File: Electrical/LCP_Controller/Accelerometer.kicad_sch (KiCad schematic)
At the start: 6 parts, among them J6 SALEAE_TEST, U10 LIS2DW12

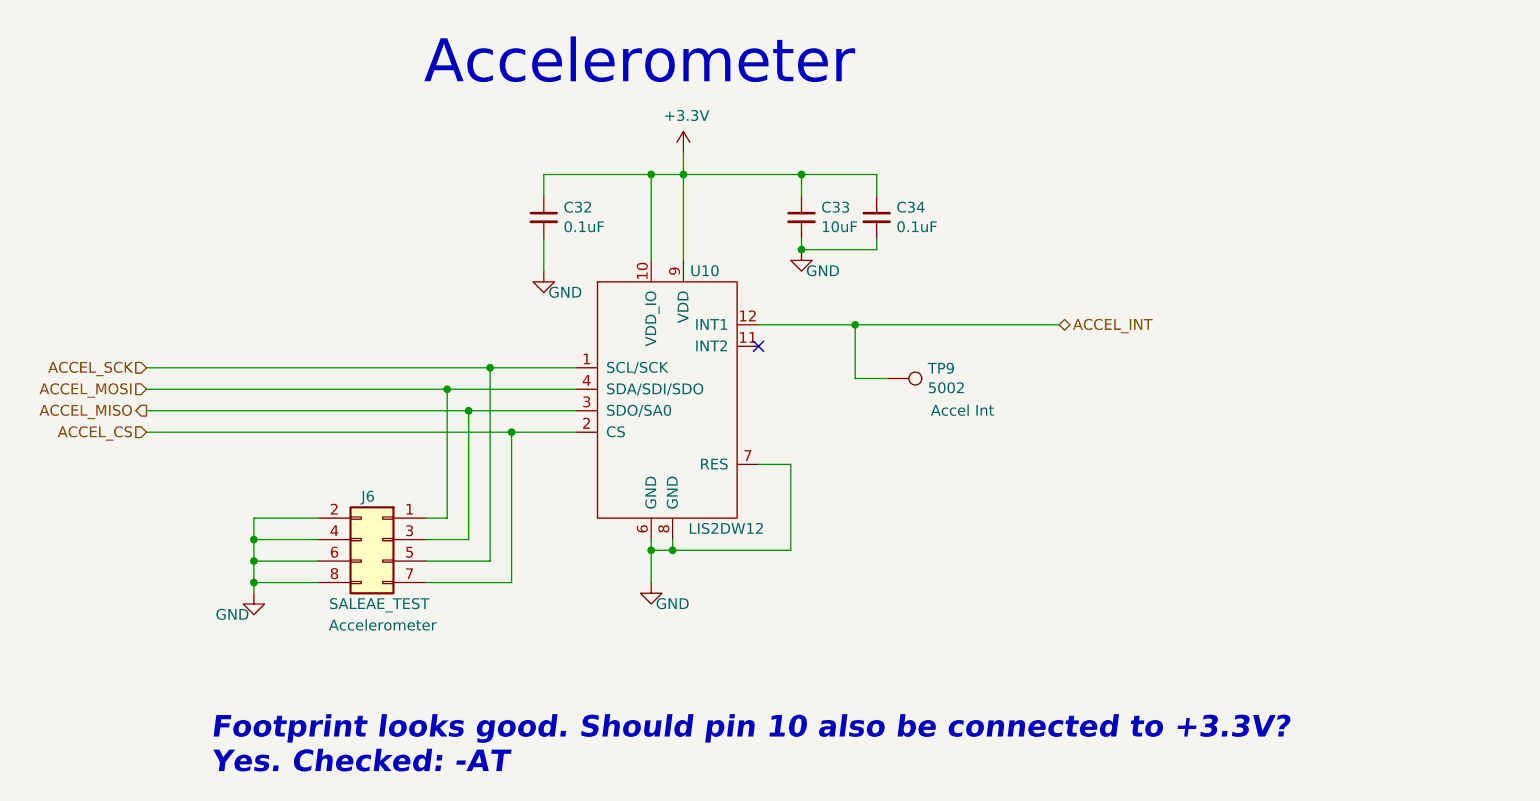
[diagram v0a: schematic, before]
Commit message: Hardware Revision : v0.3
1. modified schematic design, removed unnecessary test points.
2. pcb layout 2x8 Inches allowance dimension, layout is in progress
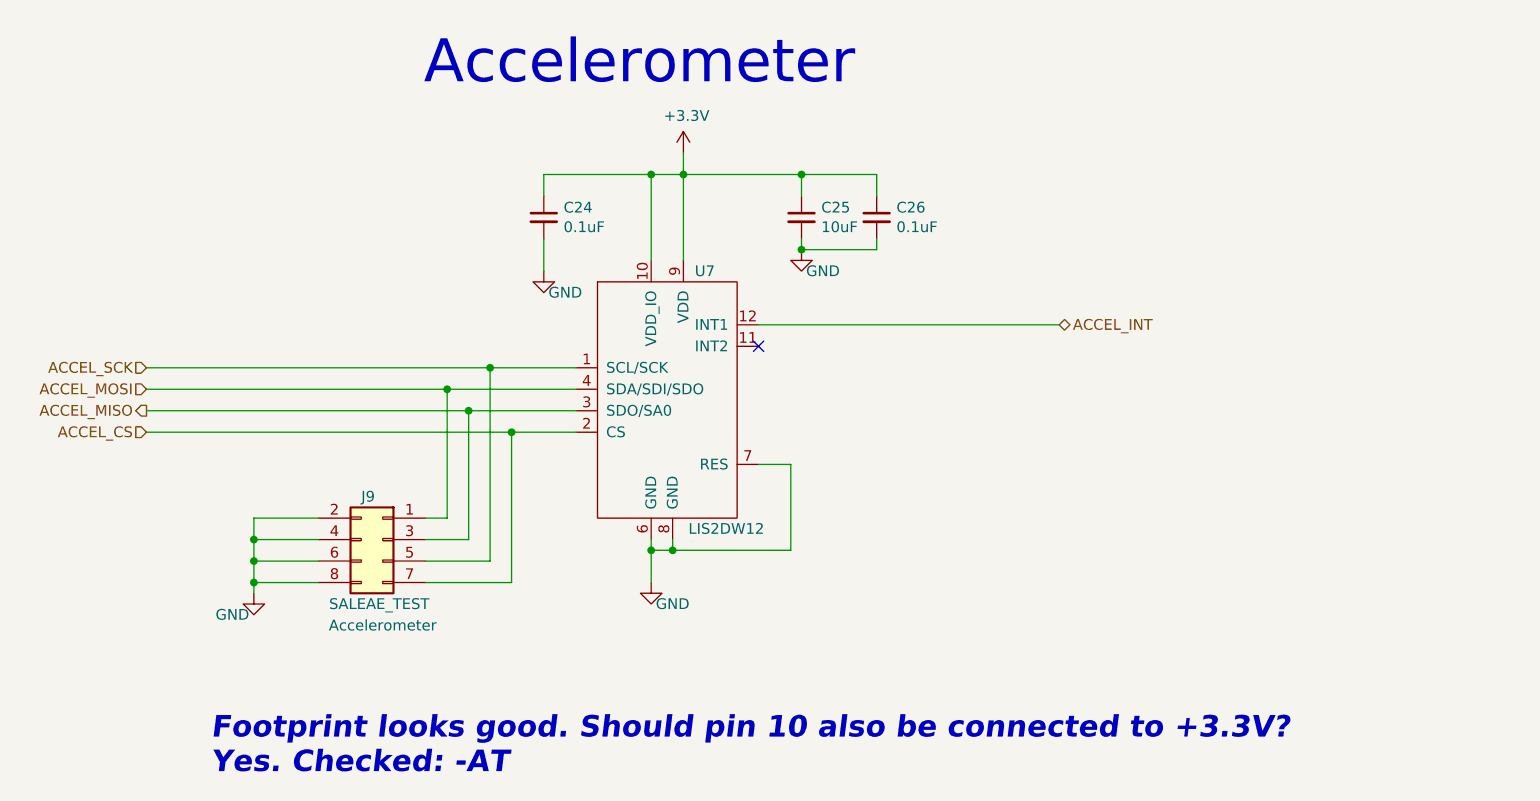
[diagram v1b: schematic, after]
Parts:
- removed TP9: 5002, TestPoint:TestPoint_Keystone_5000-5004_Miniature, symbol Connector:TestPoint
- renumbered C32 to C24, C33 to C25, C34 to C26, J6 to J9, U10 to U7
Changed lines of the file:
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@@
   (junction (at 157.48 119.38) (diameter 0) (color 0 0 0 0)
   )
-  (junction (at 179.07 92.71) (diameter 0) (color 0 0 0 0)
-  )
   (junction (at 107.95 120.65) (diameter 0) (color 0 0 0 0)
   )
@@
   )
   (no_connect (at 167.64 95.25))
-  (wire (pts (xy 182.88 99.06) (xy 179.07 99.06))
-    (stroke (width 0) (type default) (color 0 0 0 0))
-  )
   (wire (pts (xy 138.43 123.19) (xy 138.43 105.41))
     (stroke (width 0) (type default) (color 0 0 0 0))
@@
     (stroke (width 0) (type default) (color 0 0 0 0))
   )
-  (wire (pts (xy 179.07 92.71) (xy 203.2 92.71))
+  (wire (pts (xy 167.64 92.71) (xy 203.2 92.71))
     (stroke (width 0) (type default) (color 0 0 0 0))
   )
@@
     (stroke (width 0) (type default) (color 0 0 0 0))
   )
-  (wire (pts (xy 167.64 92.71) (xy 179.07 92.71))
-    (stroke (width 0) (type default) (color 0 0 0 0))
-  )
   (wire (pts (xy 181.61 74.93) (xy 181.61 77.47))
     (stroke (width 0) (type default) (color 0 0 0 0))
@@
   )
   (wire (pts (xy 95.25 102.87) (xy 133.35 102.87))
-    (stroke (width 0) (type default) (color 0 0 0 0))
-  )
-  (wire (pts (xy 179.07 99.06) (xy 179.07 92.71))
     (stroke (width 0) (type default) (color 0 0 0 0))
   )
@@
     (effects (font (size 1.27 1.27)) (justify left))
   )
-  (symbol (lib_id "Connector:TestPoint") (at 182.88 99.06 270) (unit 1)
-    (in_bom yes) (on_board yes)
-    (property "Reference" "TP9" (id 0) (at 187.6552 97.8916 90)
-      (effects (font (size 1.27 1.27)) (justify left))
-    )
-    (property "Value" "5002" (id 1) (at 187.6552 100.203 90)
-      (effects (font (size 1.27 1.27)) (justify left))
-    )
-    (property "Footprint" "TestPoint:TestPoint_Keystone_5000-5004_Miniature" (id 2) (at 182.88 104.14 0)
-      (effects (font (size 1.27 1.27)) hide)
-    )
-    (property "Datasheet" "~" (id 3) (at 182.88 104.14 0)
-      (effects (font (size 1.27 1.27)) hide)
-    )
-    (property "TestPoint" "Accel Int" (id 4) (at 191.77 102.87 90))
-    (property "MPN" "" (id 5) (at 182.88 99.06 0)
-      (effects (font (size 1.27 1.27)) hide)
-    )
-    (pin "1")
-  )
   (symbol (lib_id "Connector_Generic:Conn_02x04_Odd_Even") (at 123.19 118.11 0) (mirror y) (unit 1)
     (in_bom yes) (on_board yes)
-    (property "Reference" "J6" (id 0) (at 120.65 113.03 0)
+    (property "Reference" "J9" (id 0) (at 120.65 113.03 0)
       (effects (font (size 1.27 1.27)) (justify right))
     )
@@
   (symbol (lib_id "power:GND") (at 107.95 124.46 0) (unit 1)
     (in_bom yes) (on_board yes)
-    (property "Reference" "#PWR052" (id 0) (at 107.95 130.81 0)
+    (property "Reference" "#PWR058" (id 0) (at 107.95 130.81 0)
       (effects (font (size 1.27 1.27)) hide)
     )
@@
   (symbol (lib_id "power:GND") (at 154.94 123.19 0) (unit 1)
     (in_bom yes) (on_board yes)
-    (property "Reference" "#PWR054" (id 0) (at 154.94 129.54 0)
+    (property "Reference" "#PWR057" (id 0) (at 154.94 129.54 0)
       (effects (font (size 1.27 1.27)) hide)
     )
@@
   (symbol (lib_id "Device:C_Small") (at 142.24 80.01 0) (unit 1)
     (in_bom yes) (on_board yes)
-    (property "Reference" "C32" (id 0) (at 144.5768 78.8416 0)
+    (property "Reference" "C24" (id 0) (at 144.5768 78.8416 0)
       (effects (font (size 1.27 1.27)) (justify left))
     )
@@
   (symbol (lib_id "power:GND") (at 142.24 86.36 0) (unit 1)
     (in_bom yes) (on_board yes)
-    (property "Reference" "#PWR053" (id 0) (at 142.24 92.71 0)
+    (property "Reference" "#PWR056" (id 0) (at 142.24 92.71 0)
       (effects (font (size 1.27 1.27)) hide)
     )
@@
   (symbol (lib_id "power:+3.3V") (at 158.75 72.39 0) (unit 1)
     (in_bom yes) (on_board yes)
-    (property "Reference" "#PWR055" (id 0) (at 158.75 76.2 0)
+    (property "Reference" "#PWR054" (id 0) (at 158.75 76.2 0)
       (effects (font (size 1.27 1.27)) hide)
     )
@@
   (symbol (lib_id "PMEL_Sensors:LIS2DW12") (at 157.48 104.14 0) (unit 1)
     (in_bom yes) (on_board yes)
-    (property "Reference" "U10" (id 0) (at 161.29 86.36 0))
+    (property "Reference" "U7" (id 0) (at 161.29 86.36 0))
     (property "Value" "LIS2DW12" (id 1) (at 163.83 116.84 0))
     (property "Footprint" "Package_LGA:LGA-12_2x2mm_P0.5mm" (id 2) (at 157.48 116.84 0)
@@
   (symbol (lib_id "power:GND") (at 172.72 83.82 0) (unit 1)
     (in_bom yes) (on_board yes)
-    (property "Reference" "#PWR056" (id 0) (at 172.72 90.17 0)
+    (property "Reference" "#PWR055" (id 0) (at 172.72 90.17 0)
       (effects (font (size 1.27 1.27)) hide)
     )
@@
   (symbol (lib_id "Device:C_Small") (at 172.72 80.01 0) (unit 1)
     (in_bom yes) (on_board yes)
-    (property "Reference" "C33" (id 0) (at 175.0568 78.8416 0)
+    (property "Reference" "C25" (id 0) (at 175.0568 78.8416 0)
       (effects (font (size 1.27 1.27)) (justify left))
     )
@@
   (symbol (lib_id "Device:C_Small") (at 181.61 80.01 0) (unit 1)
     (in_bom yes) (on_board yes)
-    (property "Reference" "C34" (id 0) (at 183.9468 78.8416 0)
-      (effects (font (size 1.27 1.27)) (justify left))
-    )
+    (property "Reference" "C26" (id 0) (at 183.9468 78.8416 0)
+      (effects (font (size 1.27 1.27)) (justify left))
+    )

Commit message: Removed RF Switch
Deleted the RF Switch.

GPS Signal is routed to J17 and Iridium to J18.
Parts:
- J9: footprint Connector_PinHeader_2.54mm:PinHeader_2x04_P2.54mm_Vertical -> Connector_Molex:Molex_Micro-Fit_3.0_43045-0612_2x03_P3.00mm_Vertical

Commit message: GPS and Iridium Layout Finalized
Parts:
- J9: footprint Connector_Molex:Molex_Micro-Fit_3.0_43045-0612_2x03_P3.00mm_Vertical -> Connector_PinHeader_2.54mm:PinHeader_2x04_P2.54mm_Vertical
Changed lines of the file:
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@@
       (effects (font (size 1.27 1.27)) (justify right))
     )
-    (property "Footprint" "Connector_Molex:Molex_Micro-Fit_3.0_43045-0612_2x03_P3.00mm_Vertical" (at 123.19 118.11 0)
+    (property "Footprint" "Connector_PinHeader_2.54mm:PinHeader_2x04_P2.54mm_Vertical" (at 123.19 118.11 0)
       (effects (font (size 1.27 1.27)) hide)
     )

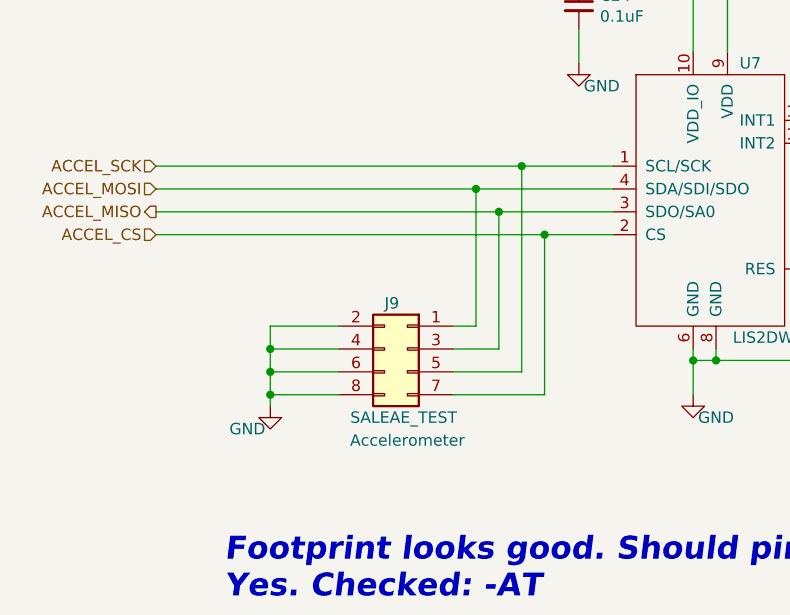
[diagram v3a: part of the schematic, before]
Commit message: Connector Progress
J2 J22 and J23 converted to Molex Microfit

SALEAE TEST connectors removed
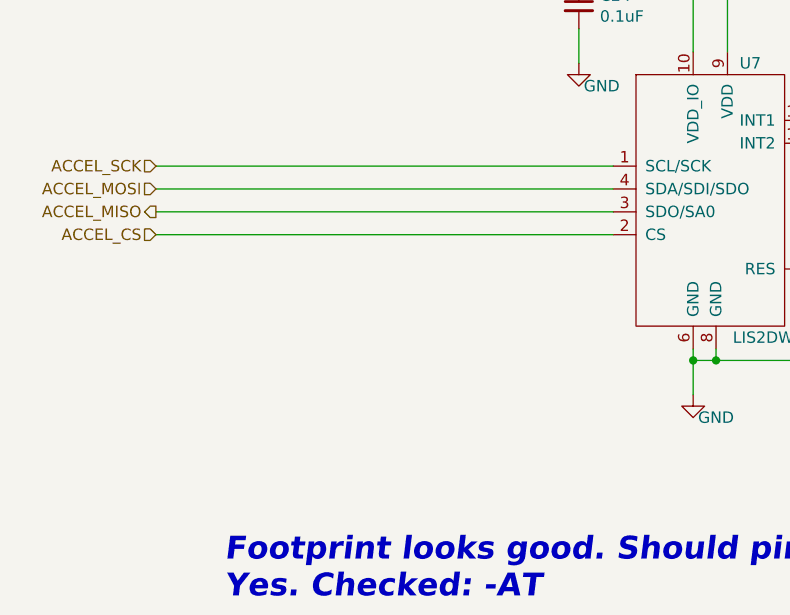
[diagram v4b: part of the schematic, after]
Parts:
- removed J9: SALEAE_TEST, Connector_PinHeader_2.54mm:PinHeader_2x04_P2.54mm_Vertical, symbol Connector_Generic:Conn_02x04_Odd_Even
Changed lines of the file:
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@@
     (comment 5 "Current design modified by: Basharat Martin")
   )
-  (junction (at 133.35 102.87) (diameter 0) (color 0 0 0 0)
-  )
-  (junction (at 135.89 97.79) (diameter 0) (color 0 0 0 0)
-  )
   (junction (at 154.94 74.93) (diameter 0) (color 0 0 0 0)
-  )
-  (junction (at 130.81 100.33) (diameter 0) (color 0 0 0 0)
-  )
-  (junction (at 107.95 123.19) (diameter 0) (color 0 0 0 0)
-  )
-  (junction (at 107.95 118.11) (diameter 0) (color 0 0 0 0)
   )
   (junction (at 172.72 83.82) (diameter 0) (color 0 0 0 0)
@@
   (junction (at 157.48 119.38) (diameter 0) (color 0 0 0 0)
   )
-  (junction (at 107.95 120.65) (diameter 0) (color 0 0 0 0)
-  )
-  (junction (at 138.43 105.41) (diameter 0) (color 0 0 0 0)
-  )
   (no_connect (at 167.64 95.25))
-  (wire (pts (xy 138.43 123.19) (xy 138.43 105.41))
-    (stroke (width 0) (type default))
-  )
   (wire (pts (xy 154.94 119.38) (xy 154.94 118.11))
     (stroke (width 0) (type default))
   )
   (wire (pts (xy 158.75 74.93) (xy 172.72 74.93))
-    (stroke (width 0) (type default))
-  )
-  (wire (pts (xy 146.05 97.79) (xy 135.89 97.79))
     (stroke (width 0) (type default))
   )
@@
     (stroke (width 0) (type default))
   )
-  (wire (pts (xy 128.27 120.65) (xy 135.89 120.65))
-    (stroke (width 0) (type default))
-  )
-  (wire (pts (xy 107.95 120.65) (xy 107.95 123.19))
-    (stroke (width 0) (type default))
-  )
   (wire (pts (xy 142.24 82.55) (xy 142.24 86.36))
-    (stroke (width 0) (type default))
-  )
-  (wire (pts (xy 107.95 115.57) (xy 115.57 115.57))
     (stroke (width 0) (type default))
   )
@@
     (stroke (width 0) (type default))
   )
-  (wire (pts (xy 107.95 118.11) (xy 107.95 115.57))
-    (stroke (width 0) (type default))
-  )
   (wire (pts (xy 142.24 74.93) (xy 142.24 77.47))
-    (stroke (width 0) (type default))
-  )
-  (wire (pts (xy 107.95 118.11) (xy 107.95 120.65))
     (stroke (width 0) (type default))
   )
@@
     (stroke (width 0) (type default))
   )
-  (wire (pts (xy 115.57 118.11) (xy 107.95 118.11))
-    (stroke (width 0) (type default))
-  )
-  (wire (pts (xy 115.57 120.65) (xy 107.95 120.65))
-    (stroke (width 0) (type default))
-  )
   (wire (pts (xy 171.45 109.22) (xy 167.64 109.22))
     (stroke (width 0) (type default))
@@
     (stroke (width 0) (type default))
   )
-  (wire (pts (xy 115.57 123.19) (xy 107.95 123.19))
-    (stroke (width 0) (type default))
-  )
   (wire (pts (xy 154.94 85.09) (xy 154.94 74.93))
     (stroke (width 0) (type default))
   )
-  (wire (pts (xy 95.25 100.33) (xy 130.81 100.33))
-    (stroke (width 0) (type default))
-  )
-  (wire (pts (xy 107.95 123.19) (xy 107.95 124.46))
+  (wire (pts (xy 95.25 100.33) (xy 146.05 100.33))
     (stroke (width 0) (type default))
   )
@@
     (stroke (width 0) (type default))
   )
-  (wire (pts (xy 130.81 115.57) (xy 130.81 100.33))
-    (stroke (width 0) (type default))
-  )
-  (wire (pts (xy 135.89 120.65) (xy 135.89 97.79))
-    (stroke (width 0) (type default))
-  )
-  (wire (pts (xy 128.27 123.19) (xy 138.43 123.19))
-    (stroke (width 0) (type default))
-  )
   (wire (pts (xy 157.48 118.11) (xy 157.48 119.38))
-    (stroke (width 0) (type default))
-  )
-  (wire (pts (xy 128.27 115.57) (xy 130.81 115.57))
     (stroke (width 0) (type default))
   )
@@
     (stroke (width 0) (type default))
   )
-  (wire (pts (xy 95.25 105.41) (xy 138.43 105.41))
-    (stroke (width 0) (type default))
-  )
-  (wire (pts (xy 146.05 100.33) (xy 130.81 100.33))
+  (wire (pts (xy 95.25 105.41) (xy 146.05 105.41))
     (stroke (width 0) (type default))
   )
@@
     (stroke (width 0) (type default))
   )
-  (wire (pts (xy 95.25 97.79) (xy 135.89 97.79))
-    (stroke (width 0) (type default))
-  )
-  (wire (pts (xy 128.27 118.11) (xy 133.35 118.11))
-    (stroke (width 0) (type default))
-  )
-  (wire (pts (xy 133.35 102.87) (xy 146.05 102.87))
+  (wire (pts (xy 95.25 97.79) (xy 146.05 97.79))
     (stroke (width 0) (type default))
   )
@@
     (stroke (width 0) (type default))
   )
-  (wire (pts (xy 95.25 102.87) (xy 133.35 102.87))
+  (wire (pts (xy 95.25 102.87) (xy 146.05 102.87))
     (stroke (width 0) (type default))
   )
   (wire (pts (xy 172.72 83.82) (xy 172.72 82.55))
-    (stroke (width 0) (type default))
-  )
-  (wire (pts (xy 133.35 118.11) (xy 133.35 102.87))
-    (stroke (width 0) (type default))
-  )
-  (wire (pts (xy 138.43 105.41) (xy 146.05 105.41))
     (stroke (width 0) (type default))
   )
@@
     (effects (font (size 1.27 1.27)) (justify left))
   )
-  (symbol (lib_id "Connector_Generic:Conn_02x04_Odd_Even") (at 123.19 118.11 0) (mirror y) (unit 1)
-    (in_bom yes) (on_board yes) (dnp no)
-    (property "Reference" "J9" (at 120.65 113.03 0)
-      (effects (font (size 1.27 1.27)) (justify right))
-    )
-    (property "Value" "SALEAE_TEST" (at 116.84 125.73 0)
-      (effects (font (size 1.27 1.27)) (justify right))
-    )
-    (property "Footprint" "Connector_PinHeader_2.54mm:PinHeader_2x04_P2.54mm_Vertical" (at 123.19 118.11 0)
-      (effects (font (size 1.27 1.27)) hide)
-    )
-    (property "Datasheet" "~" (at 123.19 118.11 0)
-      (effects (font (size 1.27 1.27)) hide)
-    )
-    (property "TestPoint" "Accelerometer" (at 123.19 128.27 0)
-      (effects (font (size 1.27 1.27)))
-    )
-    (property "MPN" "0010897080" (at 123.19 118.11 0)
-      (effects (font (size 1.27 1.27)) hide)
-    )
-    (pin "1")
-    (pin "2")
-    (pin "3")
-    (pin "4")
-    (pin "5")
-    (pin "6")
-    (pin "7")
-    (pin "8")
-    (instances
-      (project "LCP_Controller"
-        (path "/df0f358a-57ab-4ee9-8b36-6ce64ef9d813/00000000-0000-0000-0000-00005edb548e"
-          (reference "J9") (unit 1)
-        )
-      )
-    )
-  )
-  (symbol (lib_id "power:GND") (at 107.95 124.46 0) (unit 1)
-    (in_bom yes) (on_board yes) (dnp no)
-    (property "Reference" "#PWR058" (at 107.95 130.81 0)
-      (effects (font (size 1.27 1.27)) hide)
-    )
-    (property "Value" "GND" (at 105.41 127 0)
-      (effects (font (size 1.27 1.27)))
-    )
-    (property "Footprint" "" (at 107.95 124.46 0)
-      (effects (font (size 1.27 1.27)) hide)
-    )
-    (property "Datasheet" "" (at 107.95 124.46 0)
-      (effects (font (size 1.27 1.27)) hide)
-    )
-    (pin "1")
-    (instances
-      (project "LCP_Controller"
-        (path "/df0f358a-57ab-4ee9-8b36-6ce64ef9d813/00000000-0000-0000-0000-00005edb548e"
-          (reference "#PWR058") (unit 1)
-        )
-      )
-    )
-  )
   (symbol (lib_id "power:GND") (at 154.94 123.19 0) (unit 1)
